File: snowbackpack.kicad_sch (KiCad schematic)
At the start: 87 parts, among them J10 Conn_01x01_Pin, J11 Conn_01x01_Pin, J12 Conn_01x01_Pin, J13 Conn_01x01_Pin, J2 Conn_01x01_Pin, J3 Conn_01x01_Pin, J4 Conn_01x01_Pin, J5 Conn_01x01_Pin, J6 Conn_01x01_Pin, J7 Conn_01x01_Pin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

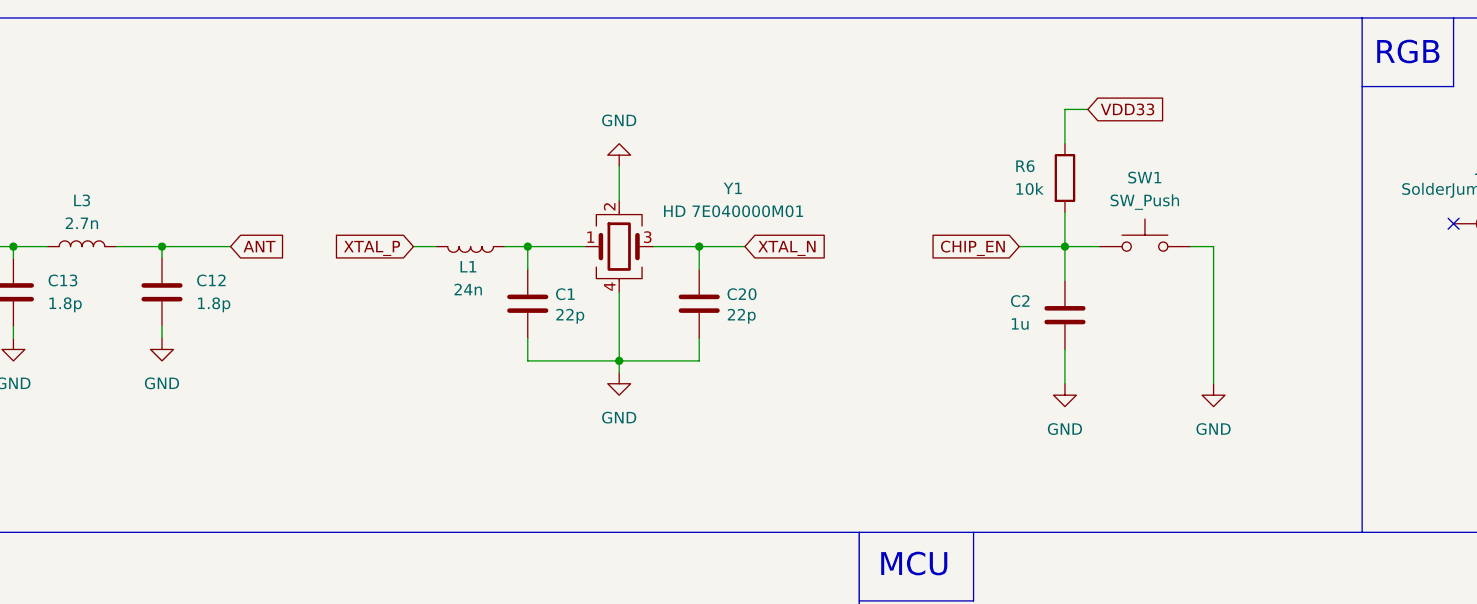
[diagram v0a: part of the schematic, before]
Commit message: First pcb routing
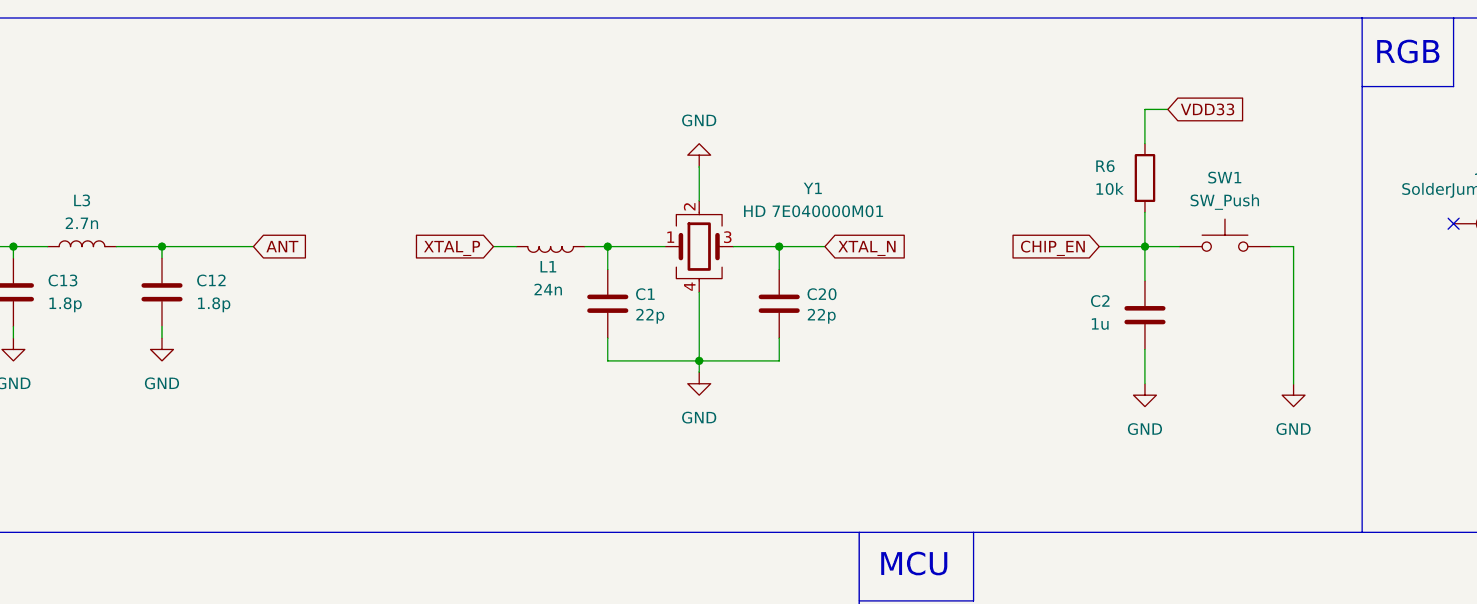
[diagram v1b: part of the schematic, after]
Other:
- moved on the sheet: C1, C2, C20, L1, R6, SW1, Y1

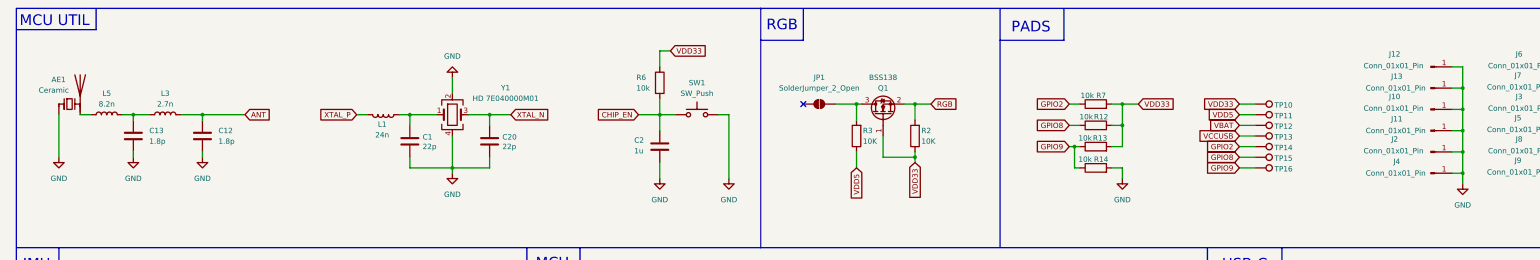
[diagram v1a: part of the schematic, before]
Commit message: Fixed smd antenna
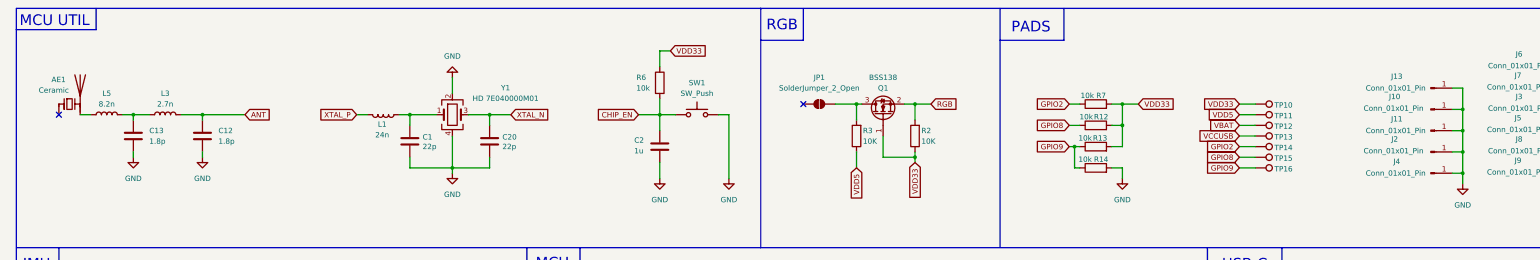
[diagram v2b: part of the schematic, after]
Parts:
- removed J12: Conn_01x01_Pin, Custom:matrix-pad-gn, symbol Connector:Conn_01x01_Pin
- AE1: footprint (none) -> Custom:CW324S
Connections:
- net GND: no longer AE1.1 (FEED)
- no-connect marks 8 -> 9
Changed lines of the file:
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@@
 	)
 	(junction
-		(at 358.14 60.96)
-		(diameter 0)
-		(color 0 0 0 0)
-	)
-	(junction
 		(at 76.2 130.81)
 		(diameter 0)
@@
 	)
 	(no_connect
+		(at 22.86 67.31)
+	)
+	(no_connect
 		(at 67.31 135.89)
 	)
@@
 	(wire
 		(pts
-			(xy 355.6 55.88) (xy 358.14 55.88)
-		)
-		(stroke
-			(width 0)
-			(type default)
-		)
-	)
-	(wire
-		(pts
 			(xy 355.6 142.24) (xy 358.14 142.24)
 		)
@@
 	(wire
 		(pts
-			(xy 358.14 55.88) (xy 358.14 60.96)
-		)
-		(stroke
-			(width 0)
-			(type default)
-		)
-	)
-	(wire
-		(pts
 			(xy 27.94 149.86) (xy 30.48 149.86)
 		)
@@
 	(wire
 		(pts
-			(xy 22.86 67.31) (xy 22.86 77.47)
-		)
-		(stroke
-			(width 0)
-			(type default)
-		)
-	)
-	(wire
-		(pts
 			(xy 384.81 68.58) (xy 384.81 71.12)
 		)
@@
 			)
 		)
-		(property "Footprint" ""
+		(property "Footprint" "Custom:CW324S"
 			(at 22.86 60.325 0)
 			(effects
@@
 	(symbol
 		(lib_id "power:GND")
-		(at 22.86 77.47 0)
-		(unit 1)
-		(exclude_from_sim no)
-		(in_bom yes)
-		(on_board yes)
-		(dnp no)
-		(fields_autoplaced yes)
-		(property "Reference" "#PWR041"
-			(at 22.86 83.82 0)
-			(effects
-				(font
-					(size 1.27 1.27)
-				)
-				(hide yes)
-			)
-		)
-		(property "Value" "GND"
-			(at 22.86 82.55 0)
-			(effects
-				(font
-					(size 1.27 1.27)
-				)
-			)
-		)
-		(property "Footprint" ""
-			(at 22.86 77.47 0)
-			(effects
-				(font
-					(size 1.27 1.27)
-				)
-				(hide yes)
-			)
-		)
-		(property "Datasheet" ""
-			(at 22.86 77.47 0)
-			(effects
-				(font
-					(size 1.27 1.27)
-				)
-				(hide yes)
-			)
-		)
-		(property "Description" "Power symbol creates a global label with name \"GND\" , ground"
-			(at 22.86 77.47 0)
-			(effects
-				(font
-					(size 1.27 1.27)
-				)
-				(hide yes)
-			)
-		)
-		(pin "1"
-		)
-		(instances
-			(project "snow-backpack"
-				(path "/35bc9aca-8f77-4570-809d-0977de13afc4"
-					(reference "#PWR041")
-					(unit 1)
-				)
-			)
-		)
-	)
-	(symbol
-		(lib_id "power:GND")
 		(at 106.68 212.09 0)
 		(unit 1)
@@
 					(unit 1)
 				)
-			)
-		)
-	)
-	(symbol
-		(lib_id "Connector:Conn_01x01_Pin")
-		(at 350.52 55.88 0)
-		(unit 1)
-		(exclude_from_sim no)
-		(in_bom yes)
-		(on_board yes)
-		(dnp no)
-		(property "Reference" "J12"
-			(at 341.884 52.832 0)
-			(effects
-				(font
-					(size 1.27 1.27)
-				)
-			)
-		)
-		(property "Value" "Conn_01x01_Pin"
-			(at 341.63 55.626 0)
-			(effects
-				(font
-					(size 1.27 1.27)
-				)
-			)
-		)
-		(property "Footprint" "Custom:matrix-pad-gn"
-			(at 350.52 55.88 0)
-			(effects
-				(font
-					(size 1.27 1.27)
-				)
-				(hide yes)
-			)
-		)
-		(property "Datasheet" "~"
-			(at 350.52 55.88 0)
-			(effects
-				(font
-					(size 1.27 1.27)
-				)
-				(hide yes)
-			)
-		)
-		(property "Description" "Generic connector, single row, 01x01, script generated"
-			(at 350.52 55.88 0)
-			(effects
-				(font
-					(size 1.27 1.27)
-				)
-				(hide yes)
-			)
-		)
-		(pin "1"
-		)
-		(instances
-			(project "snow-backpack"
-				(path "/35bc9aca-8f77-4570-809d-0977de13afc4"
-					(reference "J12")
-					(unit 1)
-				)

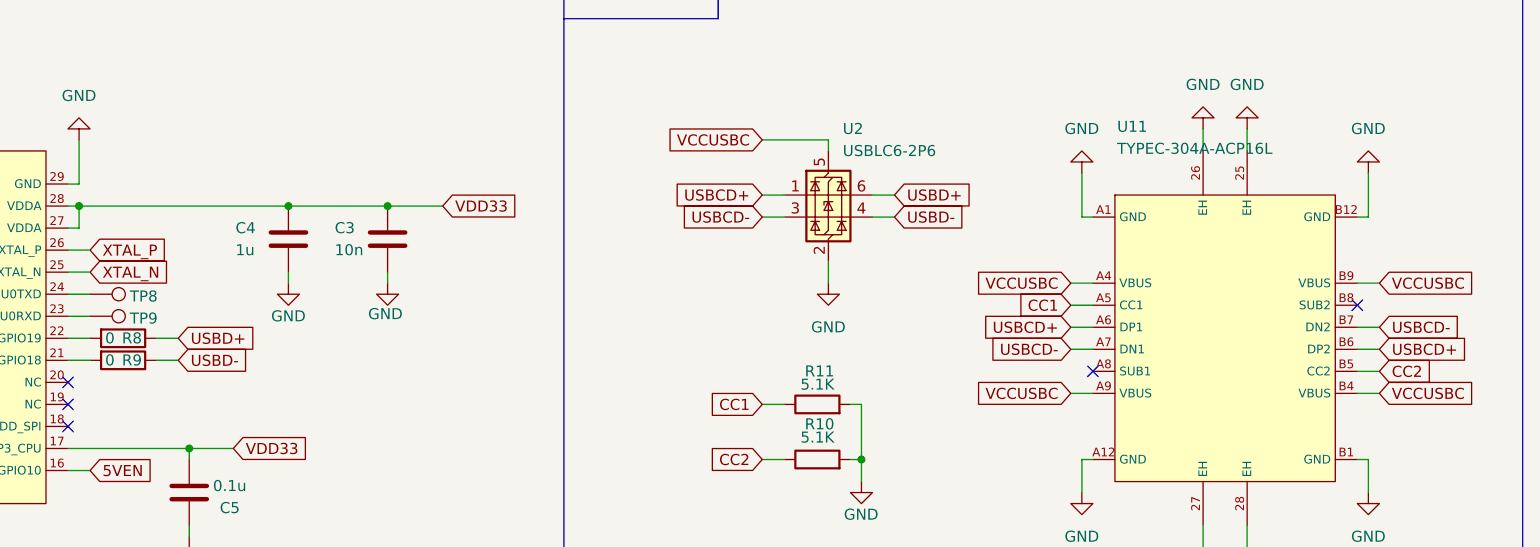
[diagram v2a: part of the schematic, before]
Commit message: Routed USB
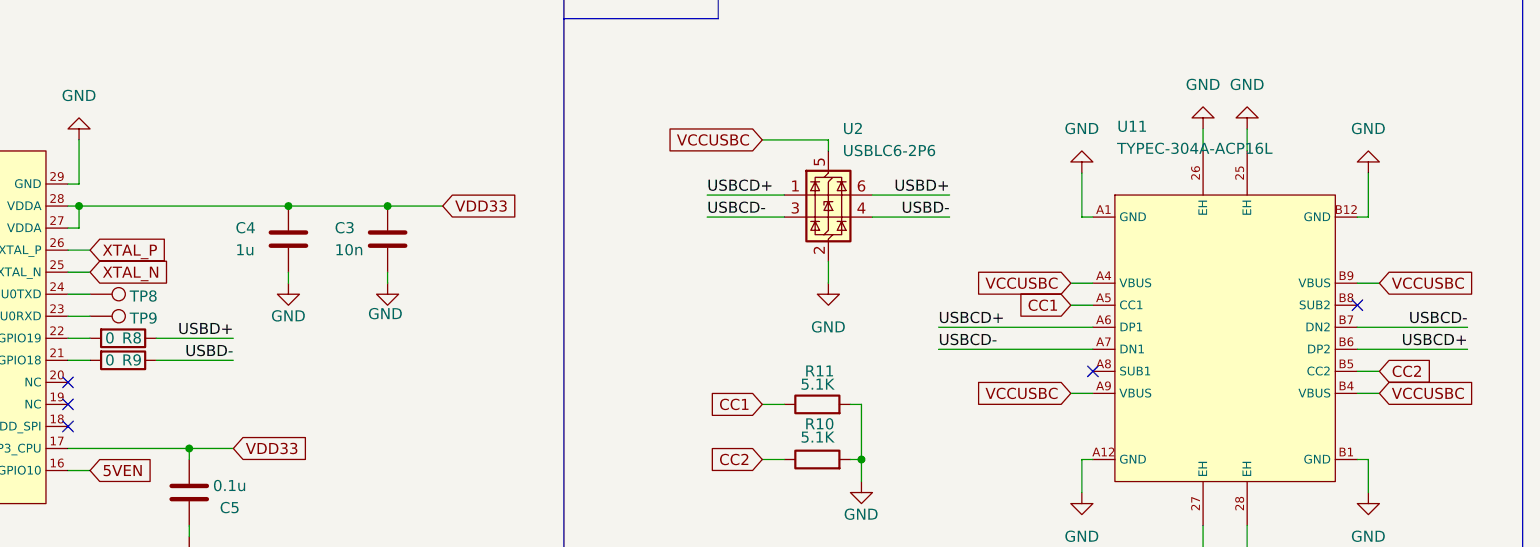
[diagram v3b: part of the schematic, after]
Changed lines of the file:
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@@
 	(wire
 		(pts
-			(xy 388.62 142.24) (xy 391.16 142.24)
+			(xy 388.62 142.24) (xy 401.32 142.24)
 		)
 		(stroke
@@
 	(wire
 		(pts
-			(xy 355.6 144.78) (xy 358.14 144.78)
-		)
-		(stroke
-			(width 0)
-			(type default)
-		)
-	)
-	(wire
-		(pts
 			(xy 31.75 133.35) (xy 31.75 140.97)
 		)
@@
 	(wire
 		(pts
-			(xy 332.74 129.54) (xy 335.28 129.54)
+			(xy 332.74 129.54) (xy 341.63 129.54)
 		)
 		(stroke
@@
 	(wire
 		(pts
-			(xy 355.6 142.24) (xy 358.14 142.24)
+			(xy 327.66 120.65) (xy 327.66 121.92)
 		)
 		(stroke
@@
 	(wire
 		(pts
-			(xy 327.66 120.65) (xy 327.66 121.92)
+			(xy 313.69 129.54) (xy 322.58 129.54)
 		)
 		(stroke
@@
 	(wire
 		(pts
-			(xy 320.04 129.54) (xy 322.58 129.54)
-		)
-		(stroke
-			(width 0)
-			(type default)
-		)
-	)
-	(wire
-		(pts
 			(xy 274.32 69.85) (xy 276.86 69.85)
 		)
@@
 	(wire
 		(pts
-			(xy 388.62 144.78) (xy 391.16 144.78)
+			(xy 388.62 144.78) (xy 401.32 144.78)
 		)
 		(stroke
@@
 	(wire
 		(pts
+			(xy 340.36 142.24) (xy 358.14 142.24)
+		)
+		(stroke
+			(width 0)
+			(type default)
+		)
+	)
+	(wire
+		(pts
 			(xy 330.2 205.74) (xy 334.01 205.74)
 		)
@@
 	(wire
 		(pts
-			(xy 332.74 127) (xy 335.28 127)
+			(xy 332.74 127) (xy 341.63 127)
 		)
 		(stroke
@@
 	(wire
 		(pts
+			(xy 313.69 127) (xy 322.58 127)
+		)
+		(stroke
+			(width 0)
+			(type default)
+		)
+	)
+	(wire
+		(pts
 			(xy 195.58 204.47) (xy 205.74 204.47)
 		)
@@
 	(wire
 		(pts
-			(xy 250.19 146.05) (xy 252.73 146.05)
+			(xy 250.19 146.05) (xy 259.08 146.05)
 		)
 		(stroke
@@
 	(wire
 		(pts
+			(xy 340.36 144.78) (xy 358.14 144.78)
+		)
+		(stroke
+			(width 0)
+			(type default)
+		)
+	)
+	(wire
+		(pts
 			(xy 388.62 149.86) (xy 391.16 149.86)
 		)
@@
 	(wire
 		(pts
-			(xy 250.19 143.51) (xy 252.73 143.51)
+			(xy 250.19 143.51) (xy 259.08 143.51)
 		)
 		(stroke
@@
 	(wire
 		(pts
-			(xy 320.04 127) (xy 322.58 127)
-		)
-		(stroke
-			(width 0)
-			(type default)
-		)
-	)
-	(wire
-		(pts
 			(xy 71.12 154.94) (xy 71.12 157.48)
 		)
@@
 		)
 	)
-	(global_label "USBCD+"
-		(shape input)
-		(at 391.16 144.78 0)
-		(fields_autoplaced yes)
+	(label "USBCD-"
+		(at 401.32 142.24 180)
 		(effects
 			(font
 				(size 1.27 1.27)
 			)
-			(justify left)
+			(justify right bottom)
 		)
-		(property "Intersheetrefs" "${INTERSHEET_REFS}"
-			(at 402.0676 144.78 0)
-			(effects
-				(font
-					(size 1.27 1.27)
-				)
-				(justify left)
-				(hide yes)
+	)
+	(label "USBD-"
+		(at 259.08 146.05 180)
+		(effects
+			(font
+				(size 1.27 1.27)
 			)
+			(justify right bottom)
+		)
+	)
+	(label "USBCD+"
+		(at 313.69 127 0)
+		(effects
+			(font
+				(size 1.27 1.27)
+			)
+			(justify left bottom)
+		)
+	)
+	(label "USBD+"
+		(at 341.63 127 180)
+		(effects
+			(font
+				(size 1.27 1.27)
+			)
+			(justify right bottom)
+		)
+	)
+	(label "USBCD+"
+		(at 401.32 144.78 180)
+		(effects
+			(font
+				(size 1.27 1.27)
+			)
+			(justify right bottom)
+		)
+	)
+	(label "USBD+"
+		(at 259.08 143.51 180)
+		(effects
+			(font
+				(size 1.27 1.27)
+			)
+			(justify right bottom)
+		)
+	)
+	(label "USBCD-"
+		(at 313.69 129.54 0)
+		(effects
+			(font
+				(size 1.27 1.27)
+			)
+			(justify left bottom)
+		)
+	)
+	(label "USBCD+"
+		(at 340.36 142.24 0)
+		(effects
+			(font
+				(size 1.27 1.27)
+			)
+			(justify left bottom)
+		)
+	)
+	(label "USBCD-"
+		(at 340.36 144.78 0)
+		(effects
+			(font
+				(size 1.27 1.27)
+			)
+			(justify left bottom)
+		)
+	)
+	(label "USBD-"
+		(at 341.63 129.54 180)
+		(effects
+			(font
+				(size 1.27 1.27)
+			)
+			(justify right bottom)
 		)
 	)
@@
 		)
 	)
-	(global_label "USBCD-"
-		(shape input)
-		(at 320.04 129.54 180)
-		(fields_autoplaced yes)
-		(effects
-			(font
-				(size 1.27 1.27)
-			)
-			(justify right)
-		)
-		(property "Intersheetrefs" "${INTERSHEET_REFS}"
-			(at 309.1324 129.54 0)
-			(effects
-				(font
-					(size 1.27 1.27)
-				)
-				(justify right)
-				(hide yes)
-			)
-		)
-	)
 	(global_label "VDD33"
 		(shape input)
@@
 		)
 	)
-	(global_label "USBCD+"
-		(shape input)
-		(at 355.6 142.24 180)
-		(fields_autoplaced yes)
-		(effects
-			(font
-				(size 1.27 1.27)
-			)
-			(justify right)
-		)
-		(property "Intersheetrefs" "${INTERSHEET_REFS}"
-			(at 344.6924 142.24 0)
-			(effects
-				(font
-					(size 1.27 1.27)
-				)
-				(justify right)
-				(hide yes)
-			)
-		)
-	)
-	(global_label "USBCD-"
-		(shape input)
-		(at 355.6 144.78 180)
-		(fields_autoplaced yes)
-		(effects
-			(font
-				(size 1.27 1.27)
-			)
-			(justify right)
-		)
-		(property "Intersheetrefs" "${INTERSHEET_REFS}"
-			(at 344.6924 144.78 0)
-			(effects
-				(font
-					(size 1.27 1.27)
-				)
-				(justify right)
-				(hide yes)
-			)
-		)
-	)
-	(global_label "USBCD+"
-		(shape input)
-		(at 320.04 127 180)
-		(fields_autoplaced yes)
-		(effects
-			(font
-				(size 1.27 1.27)
-			)
-			(justify right)
-		)
-		(property "Intersheetrefs" "${INTERSHEET_REFS}"
-			(at 309.1324 127 0)
-			(effects
-				(font
-					(size 1.27 1.27)
-				)
-				(justify right)
-				(hide yes)
-			)
-		)
-	)
 	(global_label "GPIO8"
 		(shape input)
@@
 		)
 	)
-	(global_label "USBD+"
-		(shape input)
-		(at 335.28 127 0)
-		(fields_autoplaced yes)
-		(effects
-			(font
-				(size 1.27 1.27)
-			)
-			(justify left)
-		)
-		(property "Intersheetrefs" "${INTERSHEET_REFS}"
-			(at 344.9176 127 0)
-			(effects
-				(font
-					(size 1.27 1.27)
-				)
-				(justify left)
-				(hide yes)
-			)
-		)
-	)
 	(global_label "CC2"
 		(shape input)
@@
 		)
 	)
-	(global_label "USBD-"
-		(shape input)
-		(at 335.28 129.54 0)
-		(fields_autoplaced yes)
-		(effects
-			(font
-				(size 1.27 1.27)
-			)
-			(justify left)
-		)
-		(property "Intersheetrefs" "${INTERSHEET_REFS}"
-			(at 344.9176 129.54 0)
-			(effects
-				(font
-					(size 1.27 1.27)
-				)
-				(justify left)
-				(hide yes)
-			)
-		)
-	)
 	(global_label "VDD33"
 		(shape input)
@@
 		)
 	)
-	(global_label "USBCD-"
-		(shape input)
-		(at 391.16 142.24 0)
-		(fields_autoplaced yes)
-		(effects
-			(font
-				(size 1.27 1.27)
-			)
-			(justify left)
-		)
-		(property "Intersheetrefs" "${INTERSHEET_REFS}"
-			(at 402.0676 142.24 0)
-			(effects
-				(font
-					(size 1.27 1.27)
-				)
-				(justify left)
-				(hide yes)
-			)
-		)
-	)
 	(global_label "VDD33"
 		(shape input)
@@
 		)
 	)
-	(global_label "USBD+"
-		(shape input)
-		(at 252.73 143.51 0)
-		(fields_autoplaced yes)
-		(effects
-			(font
-				(size 1.27 1.27)
-			)
-			(justify left)
-		)
-		(property "Intersheetrefs" "${INTERSHEET_REFS}"
-			(at 262.3676 143.51 0)
-			(effects
-				(font
-					(size 1.27 1.27)
-				)
-				(justify left)
-				(hide yes)
-			)
-		)
-	)
 	(global_label "SCL"
 		(shape input)
@@
 			(effects
 				(font
-					(size 1.27 1.27)
-				)
-				(justify left)
-				(hide yes)
-			)
-		)
-	)
-	(global_label "USBD-"
-		(shape input)
-		(at 252.73 146.05 0)
-		(fields_autoplaced yes)
-		(effects
-			(font
-				(size 1.27 1.27)
-			)
-			(justify left)
-		)
-		(property "Intersheetrefs" "${INTERSHEET_REFS}"
-			(at 262.3676 146.05 0)
-			(effects
-				(font

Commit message: Added v1 gerber files
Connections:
- net USBCD+: now also U2.3 (I/O2); no longer U2.1 (I/O1)
- net USBCD-: now also U2.1 (I/O1); no longer U2.3 (I/O2)
- net USBD+: now also U2.4 (I/O2); no longer U2.6 (I/O1)
- net USBD-: now also U2.6 (I/O1); no longer U2.4 (I/O2)
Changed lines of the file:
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@@
 	)
 	(label "USBCD+"
-		(at 313.69 127 0)
+		(at 313.69 129.54 0)
 		(effects
 			(font
@@
 	)
 	(label "USBD+"
-		(at 341.63 127 180)
+		(at 341.63 129.54 180)
 		(effects
 			(font
@@
 	)
 	(label "USBCD-"
-		(at 313.69 129.54 0)
+		(at 313.69 127 0)
 		(effects
 			(font
@@
 	)
 	(label "USBD-"
-		(at 341.63 129.54 180)
+		(at 341.63 127 180)
 		(effects
 			(font

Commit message: added BOM and cleaned up schematics
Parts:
- C10, C5, C8: value 0.1u -> 100n
- JP2: now left out of the parts list
- R10, R11: value 5.1K -> 5.1k
- R15, R2, R3, R5: value 10K -> 10k
- R4: value 5K -> 5k

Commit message: Updated BOM
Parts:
- J10, J11, J13, J2, J3, J4, J5, J6, J7, J8, J9, TP10, TP11, TP12, TP13, TP14, TP15, TP16: now left out of the parts list
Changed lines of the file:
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@@
 		(unit 1)
 		(exclude_from_sim no)
-		(in_bom yes)
+		(in_bom no)
 		(on_board yes)
 		(dnp no)
@@
 		(unit 1)
 		(exclude_from_sim no)
-		(in_bom yes)
+		(in_bom no)
 		(on_board yes)
 		(dnp no)
@@
 		(unit 1)
 		(exclude_from_sim no)
-		(in_bom yes)
+		(in_bom no)
 		(on_board yes)
 		(dnp no)
@@
 		(unit 1)
 		(exclude_from_sim no)
-		(in_bom yes)
+		(in_bom no)
 		(on_board yes)
 		(dnp no)
@@
 		(unit 1)
 		(exclude_from_sim no)
-		(in_bom yes)
+		(in_bom no)
 		(on_board yes)
 		(dnp no)
@@
 		(unit 1)
 		(exclude_from_sim no)
-		(in_bom yes)
+		(in_bom no)
 		(on_board yes)
 		(dnp no)
@@
 		(unit 1)
 		(exclude_from_sim no)
-		(in_bom yes)
+		(in_bom no)
 		(on_board yes)
 		(dnp no)
@@
 		(unit 1)
 		(exclude_from_sim no)
-		(in_bom yes)
+		(in_bom no)
 		(on_board yes)
 		(dnp no)
@@
 		(unit 1)
 		(exclude_from_sim no)
-		(in_bom yes)
+		(in_bom no)
 		(on_board yes)
 		(dnp no)
@@
 		(unit 1)
 		(exclude_from_sim no)
-		(in_bom yes)
+		(in_bom no)
 		(on_board yes)
 		(dnp no)
@@
 		(unit 1)
 		(exclude_from_sim no)
-		(in_bom yes)
+		(in_bom no)
 		(on_board yes)
 		(dnp no)
@@
 		(unit 1)
 		(exclude_from_sim no)
-		(in_bom yes)
+		(in_bom no)
 		(on_board yes)
 		(dnp no)
@@
 		(unit 1)
 		(exclude_from_sim no)
-		(in_bom yes)
+		(in_bom no)
 		(on_board yes)
 		(dnp no)
@@
 		(unit 1)
 		(exclude_from_sim no)
-		(in_bom yes)
+		(in_bom no)
 		(on_board yes)
 		(dnp no)
@@
 		(unit 1)
 		(exclude_from_sim no)
-		(in_bom yes)
+		(in_bom no)
 		(on_board yes)
 		(dnp no)
@@
 		(unit 1)
 		(exclude_from_sim no)
-		(in_bom yes)
+		(in_bom no)
 		(on_board yes)
 		(dnp no)
@@
 		(unit 1)
 		(exclude_from_sim no)
-		(in_bom yes)
+		(in_bom no)
 		(on_board yes)
 		(dnp no)
@@
 		(unit 1)
 		(exclude_from_sim no)
-		(in_bom yes)
+		(in_bom no)
 		(on_board yes)
 		(dnp no)
